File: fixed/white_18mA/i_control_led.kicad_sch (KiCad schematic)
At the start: 14 parts, among them J1 Conn_01x04, J2 Conn_01x04, Q1 MMBT5551L, U1 LM2775DSG, U2 LMV321

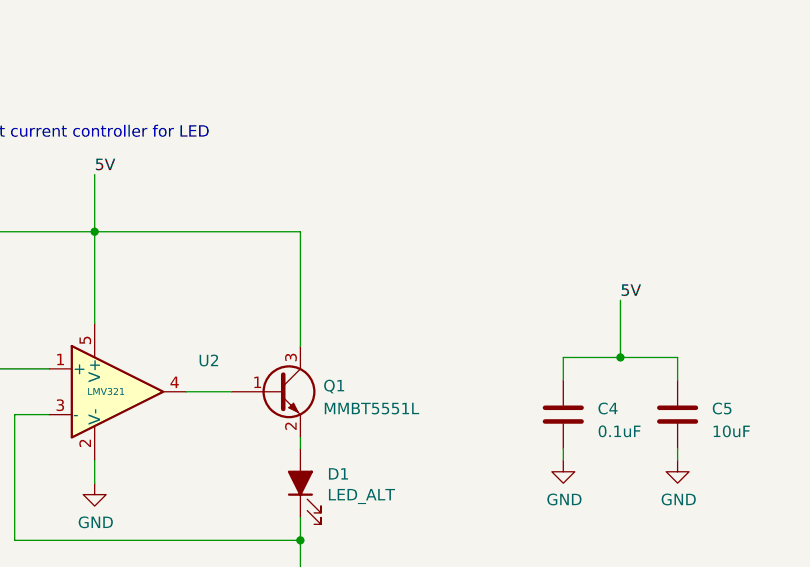
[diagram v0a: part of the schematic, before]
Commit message: Added spice sims (preliminary).
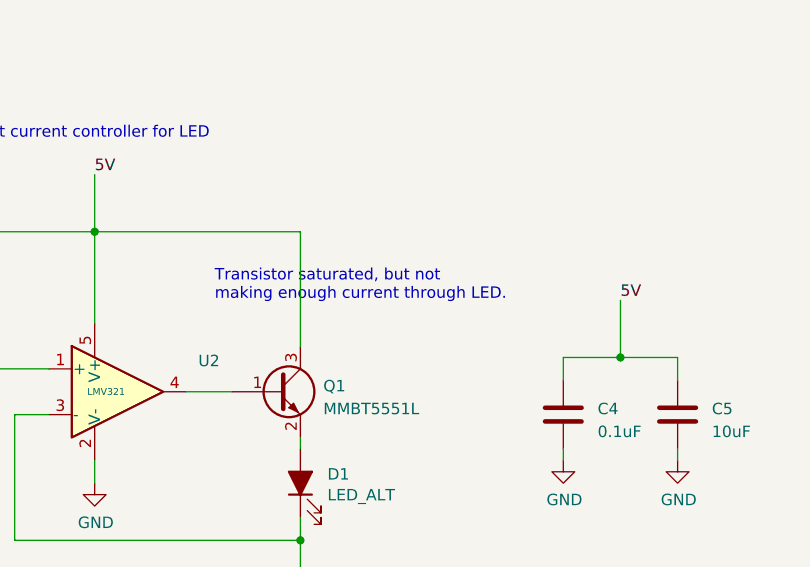
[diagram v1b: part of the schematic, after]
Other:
- note added: "Transistor saturated, but not making enough current through LED."
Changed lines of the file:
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@@
+    (effects (font (size 1.27 1.27)) (justify left bottom))
+  )
+  (text "Transistor saturated, but not \nmaking enough current through LED."
+    (at 151.765 76.327 0)
     (effects (font (size 1.27 1.27)) (justify left bottom))
   )
